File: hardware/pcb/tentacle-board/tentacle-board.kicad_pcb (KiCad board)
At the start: 2 copper layers, 110.9 x 55 mm, 74 parts, among them J1 USB_B_Micro, J2 Conn_01x02, J5 Motor, J6 Motor, U1 NCP1117-3.3_SOT223, U2 W25Q128JVS, U3 RP2040, U4 DRV8825PWP, U5 DRV8825PWP, Y1 ABLS-12.000MHZ-B4-T

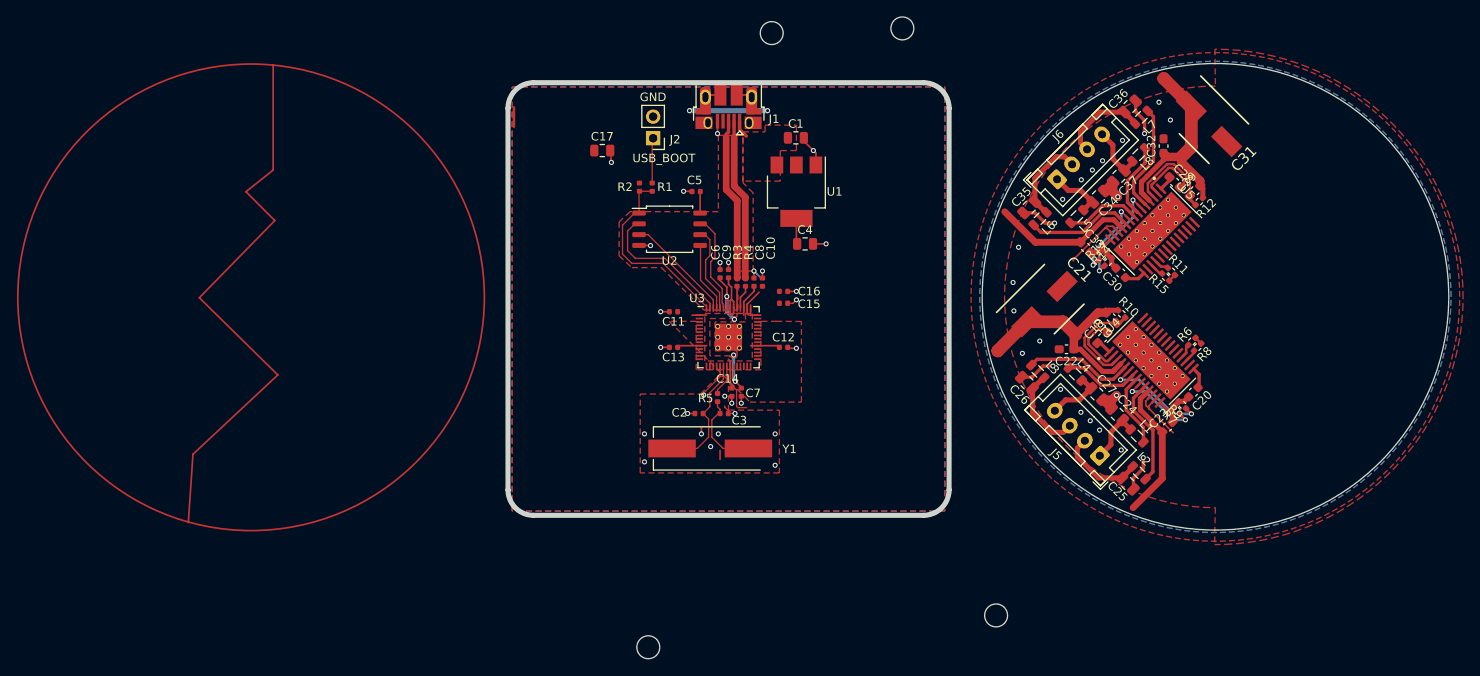
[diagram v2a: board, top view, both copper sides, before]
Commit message: Added the MCU and supporting components and wired them up
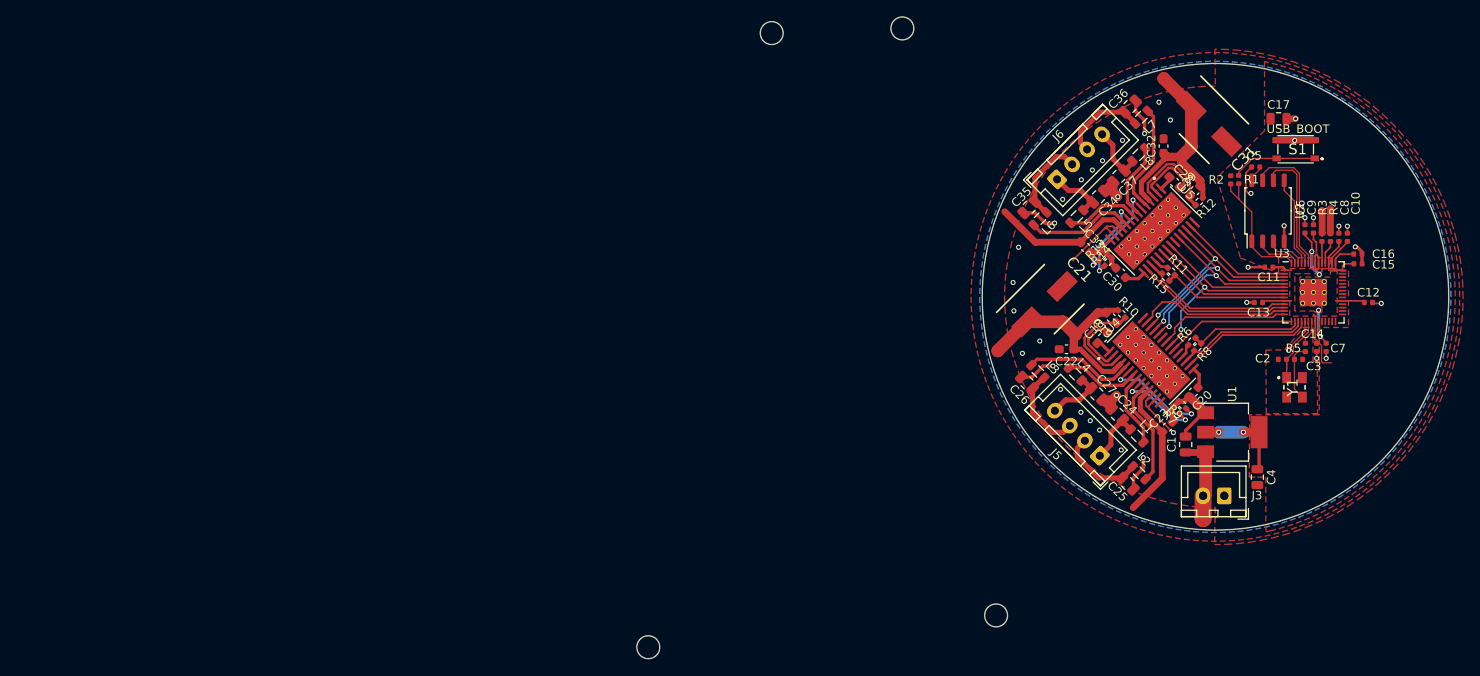
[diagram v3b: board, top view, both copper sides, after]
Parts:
- removed J1: USB_B_Micro, RP2040_minimal:USB_Micro-B_Amphenol_10103594-0001LF_Horizontal_modified
- removed J2: Conn_01x02, Connector_PinHeader_2.54mm:PinHeader_1x02_P2.54mm_Vertical
- added J3: Conn_01x02, Connector_JST:JST_XH_B2B-XH-A_1x02_P2.50mm_Vertical, F.Cu at (158.4, 118.7)
- added S1: PTS815_SJM_250_SMTR_LFS, tentacle-board:PTS815SJM250SMTRLFS, F.Cu at (166.9, 77.8)
- Y1: value ABLS-12.000MHZ-B4-T -> ABM8-12.000MHZ-20-B1U-T; footprint RP2040_minimal:Crystal_SMD_HC49-US -> tentacle-board:ABM810000MHZ12D2W
- moved C17 79.8 mm to (164.8, 74.2)
- moved U2 70.6 mm to (163.6, 85.1), turned to 90 degrees
- moved C11 70.4 mm to (163.7, 91.8)
- moved R2 69.7 mm to (159.2, 81.5)
- moved R5 69.5 mm to (168.0, 101.2)
- moved Y1 69.3 mm to (166.7, 105.9), turned to -90 degrees
- moved C12 69.2 mm to (175.4, 95.9)
- moved C13 69.2 mm to (162.5, 95.9)
- moved C10 69.2 mm to (173.0, 88.2)
- moved C14 69.2 mm to (169.3, 101.2)
- moved C6 69.2 mm to (168.0, 87.2)
- moved C7 69.2 mm to (170.5, 101.2)
- moved C8 69.2 mm to (172.0, 88.2)
- moved C9 69.2 mm to (169.0, 87.2)
- moved R3 69.2 mm to (170.0, 88.2)
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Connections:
- C1 pad 1: VBUS -> VDC
- C14 pad 2: unconnected-(C14-Pad2) -> GND
- C19 pad 2: VMM -> VDC
- C21 pad 1: VMM -> VDC
- C22 pad 1: VMM -> VDC
- C23 pad 1: VMM -> VDC
- C29 pad 2: VMM -> VDC
- C3 pad 1: Net-(C3-Pad1) -> Net-(Y1-X2)
- C31 pad 1: VMM -> VDC
- C32 pad 1: VMM -> VDC
- C33 pad 1: VMM -> VDC
- R10 pad 1: VMM -> VDC
- R11 pad 2: /Motor Driver1/FAULT -> /GPIO7
- R12 pad 1: VMM -> VDC
- R15 pad 1: /Motor Driver1/FAULT -> /GPIO7
- R15 pad 2: /Motor Driver1/SLP -> /GPIO8
- R5 pad 2: Net-(C3-Pad1) -> Net-(Y1-X2)
- R6 pad 2: /Motor Driver/FAULT -> /GPIO13
- R8 pad 1: /Motor Driver/FAULT -> /GPIO13
- R8 pad 2: /Motor Driver/SLP -> /GPIO14
- U1 pad 3: VBUS -> VDC
- U4 pad 11: VMM -> VDC
- U4 pad 16: /Motor Driver/RESET -> /GPIO15
- U4 pad 17: /Motor Driver/SLP -> /GPIO14
- U4 pad 20: /Motor Driver/DIR -> /GPIO12
- U4 pad 21: /Motor Driver/ENABLE -> /GPIO5
- U4 pad 22: /Motor Driver/STEP -> /GPIO11
- U4 pad 24: /Motor Driver/MODE0 -> /GPIO3
- U4 pad 25: /Motor Driver/MODE1 -> /GPIO2
- U4 pad 26: /Motor Driver/MODE2 -> /GPIO1
- U4 pad 27: /Motor Driver/HOME -> /GPIO10
- U4 pad 4: VMM -> VDC
- U5 pad 11: VMM -> VDC
- U5 pad 16: /Motor Driver1/RESET -> /GPIO9
- U5 pad 17: /Motor Driver1/SLP -> /GPIO8
- U5 pad 20: /Motor Driver1/DIR -> /GPIO6
- U5 pad 21: /Motor Driver1/ENABLE -> /GPIO5
- U5 pad 22: /Motor Driver1/STEP -> /GPIO4
- U5 pad 24: /Motor Driver1/MODE0 -> /GPIO3
- U5 pad 25: /Motor Driver1/MODE1 -> /GPIO2
- U5 pad 26: /Motor Driver1/MODE2 -> /GPIO1
- U5 pad 27: /Motor Driver1/HOME -> /GPIO0
- U5 pad 4: VMM -> VDC
- Y1 pad 2: Net-(C3-Pad1) -> GND
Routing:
- net VDC: track 0.00 -> 96.3 mm
- net VMM: track 85.9 -> 0.00 mm
- net /GPIO3: track 0.00 -> 25.3 mm, vias 0 -> 2
- net /GPIO2: track 0.00 -> 25.2 mm, vias 0 -> 2
- net /GPIO1: track 0.00 -> 25.0 mm, vias 0 -> 2
- net /GPIO5: track 0.00 -> 24.4 mm, vias 0 -> 2
- net /GPIO8: track 0.00 -> 18.4 mm
- net /GPIO9: track 0.00 -> 18.4 mm
- net /GPIO10: track 0.00 -> 18.3 mm
- net /USB_D+: track 19.2 -> 2.70 mm
- net /GPIO11: track 0.00 -> 16.3 mm
- net /GPIO6: track 0.00 -> 16.2 mm
- net /USB_D-: track 19.1 -> 2.88 mm
- net /GPIO14: track 0.00 -> 15.9 mm
- net /GPIO15: track 0.00 -> 15.7 mm
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- added copper zone on F.Cu, net VDC
- removed copper zone on F.Cu, net VBUS
- removed copper zone on F.Cu, net VMM
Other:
- board size 110.9 x 55 mm -> 55 x 55 mm
- board text removed: "GND"

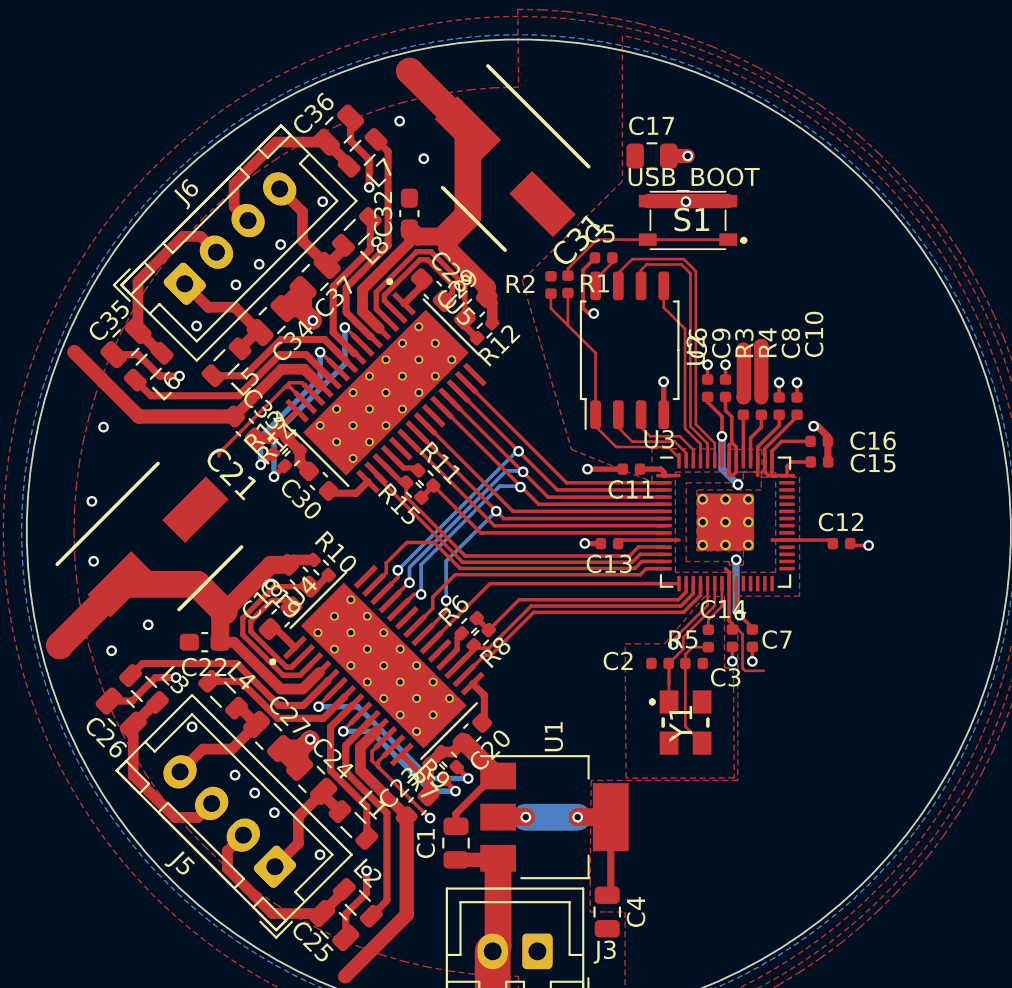
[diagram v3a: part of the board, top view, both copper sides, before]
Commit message: Updated flash to a smaller package, moved in the MCU to make some more room
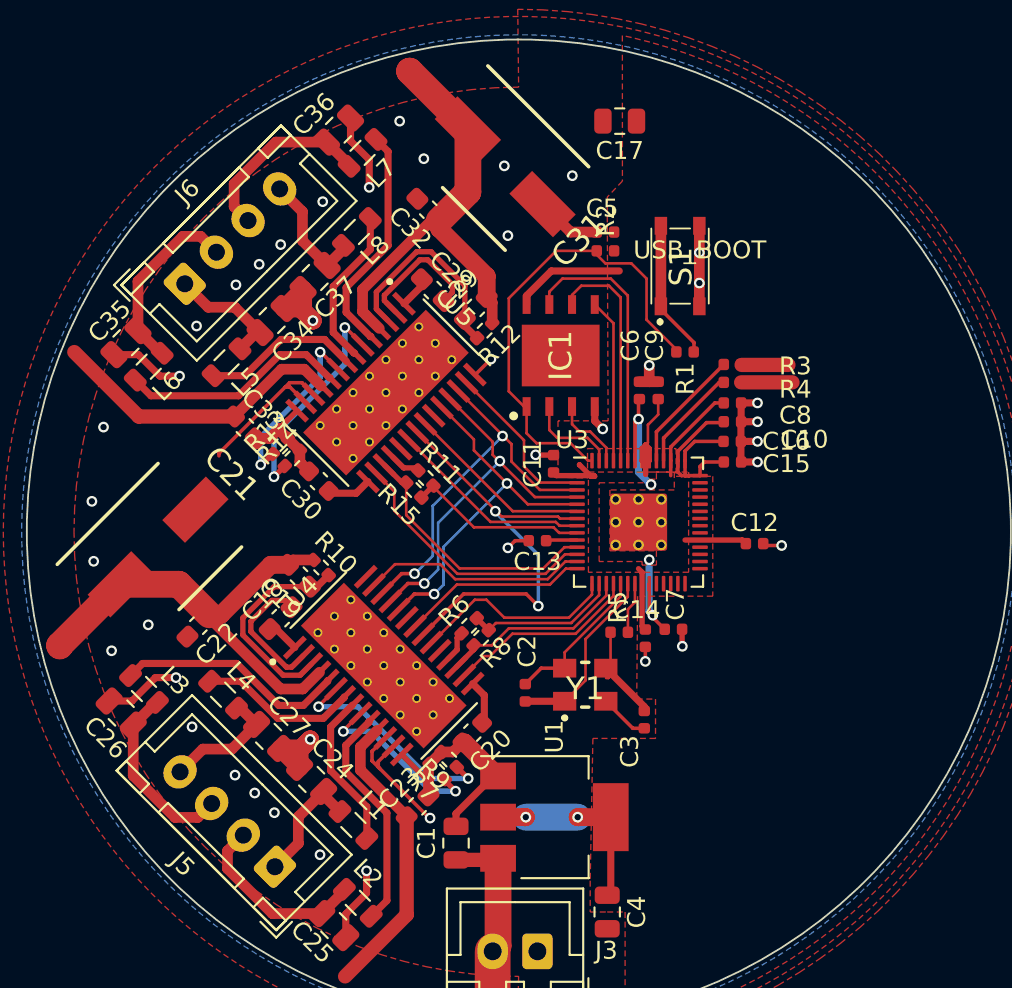
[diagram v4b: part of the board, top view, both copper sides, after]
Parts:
- removed U2: W25Q128JVS, Package_SO:SOIC-8_5.23x5.23mm_P1.27mm
- added IC1: W25Q32JVZPIQ, tentacle-board:SON127P600X500X80-9N-D, F.Cu at (159.7, 85.4)
- moved C2 7.71 mm to (157.8, 104.2), turned to 90 degrees
- moved R1 7.56 mm to (166.7, 85.2), turned to 0 degrees
- moved Y1 5.99 mm to (161.1, 103.8), turned to 0 degrees
- moved R5 4.99 mm to (163.0, 100.9), turned to 180 degrees
- moved C12 4.86 mm to (170.6, 95.9)
- moved C15 4.86 mm to (169.3, 91.3)
- moved C16 4.86 mm to (169.3, 90.2)
- moved C14 4.86 mm to (164.5, 101.2)
- moved U3 4.86 mm to (164.1, 94.7)
- moved C7 4.44 mm to (166.0, 100.7), turned to 0 degrees
- moved C11 4.36 mm to (159.3, 91.5), turned to 90 degrees
- moved C3 4.19 mm to (164.4, 105.7), turned to -90 degrees
- moved C13 4.03 mm to (158.4, 95.8)
- moved C6 3.81 mm to (164.1, 87.3)
- moved C9 3.76 mm to (165.2, 87.3)
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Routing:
- net /QSPI_SS: track 16.6 -> 26.7 mm
- net GND: track 76.7 -> 86.5 mm, vias 38 -> 40
- net +3V3: track 48.2 -> 54.4 mm
- net /GPIO11: track 16.3 -> 10.4 mm
- net /GPIO10: track 18.3 -> 12.6 mm
- net /GPIO3: track 25.3 -> 20.4 mm
- net /GPIO14: track 15.9 -> 11.0 mm
- net /GPIO6: track 16.2 -> 11.4 mm
- net /GPIO4: track 15.4 -> 10.5 mm
- net /GPIO15: track 15.7 -> 10.9 mm
- net /GPIO7: track 14.9 -> 10.1 mm
- net /GPIO13: track 13.3 -> 8.57 mm
- net Net-(U3-USB_DP): track 2.56 -> 6.93 mm
- net /GPIO2: track 25.2 -> 20.8 mm
- net /GPIO0: track 13.3 -> 9.34 mm
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
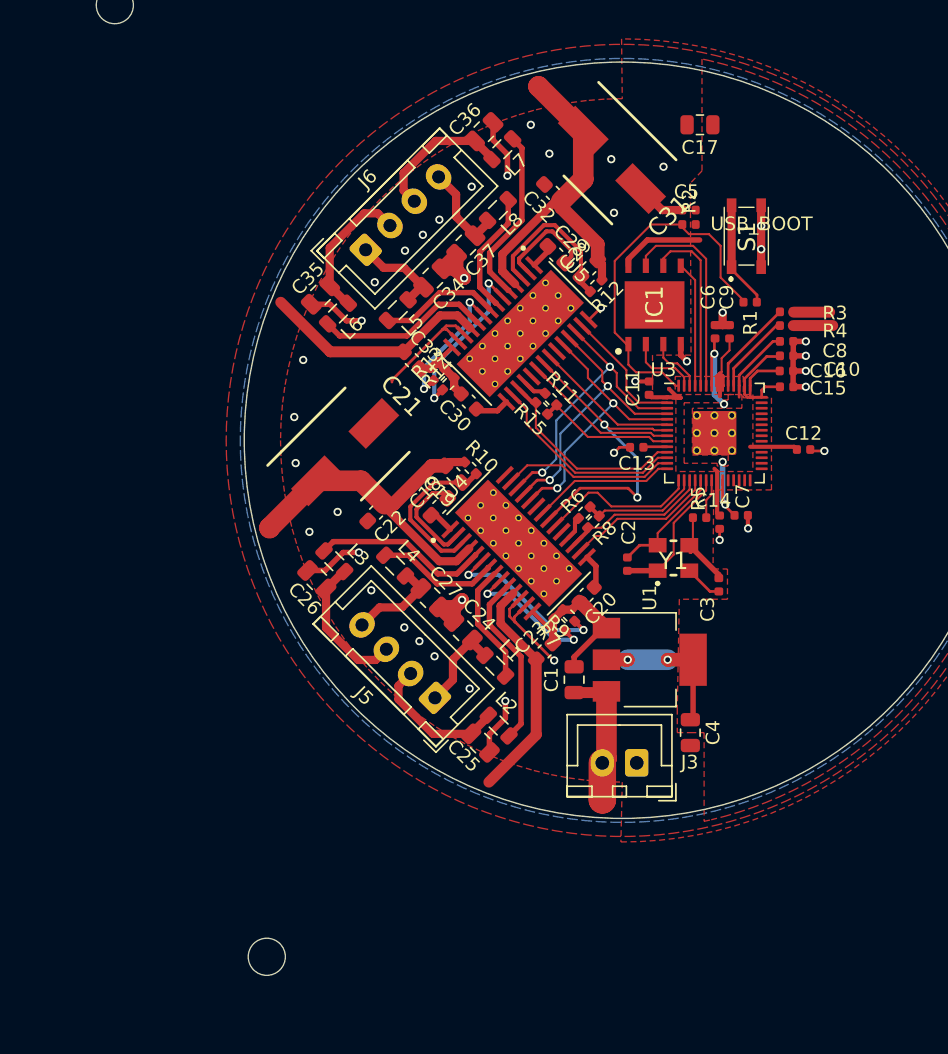
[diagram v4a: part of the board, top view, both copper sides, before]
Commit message: Updated references and formatted silkscreen layer
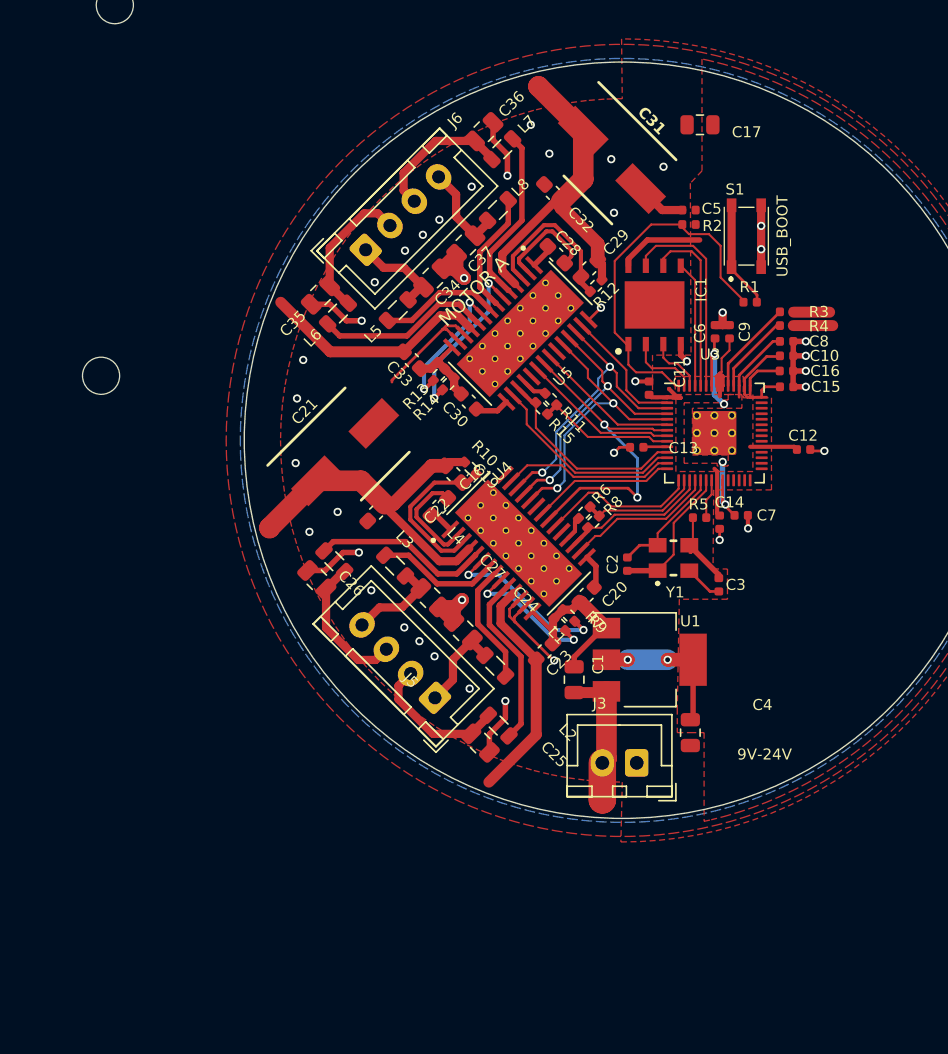
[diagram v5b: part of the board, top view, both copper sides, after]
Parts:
- moved H3 43.9 mm to (119.5, 90.5)
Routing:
- net /GPIO3: track 20.4 -> 21.1 mm
